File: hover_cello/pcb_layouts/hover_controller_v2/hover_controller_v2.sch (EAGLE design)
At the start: 32 parts, among them IC1 74LS279N, U1 L298

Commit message: placed all parts in .brd, started preliminary routing
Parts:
- added RN2: (no value), resistor-net:RN09
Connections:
- removed net N$10: CONTROL_IN.6, IC1C.R
- removed net N$11: CONTROL_IN.7, IC1D.S
- removed net N$12: CONTROL_IN.8, IC1D.R
- removed net N$5 (its old number): CONTROL_IN.1, IC1A.S1
- removed net N$6: CONTROL_IN.2, IC1A.R
- removed net N$7: CONTROL_IN.3, IC1B.S1
- removed net N$8: CONTROL_IN.4, IC1B.R
- removed net N$9: CONTROL_IN.5, IC1C.S
- new net R1: CONTROL_IN.2, IC1A.R, RN2.3
- new net R2: CONTROL_IN.4, IC1B.R, RN2.9
- new net R3: CONTROL_IN.6, IC1C.R, RN2.6
- new net R4: CONTROL_IN.8, IC1D.R, RN2.5
- new net S1: CONTROL_IN.1, IC1A.S1, RN2.2
- new net S2: CONTROL_IN.3, IC1B.S1, RN2.8
- new net S3: CONTROL_IN.5, IC1C.S, RN2.7
- new net S4: CONTROL_IN.7, IC1D.S, RN2.4
- net GND: now also VR1.1, VR2.1; no longer VR1.3, VR2.3
- net VCC: now also RN2.1, VR1.3, VR2.3; no longer VR1.1, VR2.1
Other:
- moved on the sheet: VR1, VR2
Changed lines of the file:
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@@
 <part name="C5" library="SparkFun-Capacitors" deviceset="CAP_POL" device="PTH2" value="220µf"/>
 <part name="GND15" library="SparkFun-Aesthetics" deviceset="GND" device=""/>
+<part name="RN2" library="resistor-net" library_urn="urn:adsk.eagle:library:343" deviceset="RN09" device=""/>
+<part name="SUPPLY9" library="SparkFun-Aesthetics" deviceset="VCC" device=""/>
 </parts>
 <sheets>
@@
 <instance part="U$1" gate="G$1" x="248.92" y="66.04" rot="R180"/>
 <instance part="POWER" gate="G$1" x="66.04" y="53.34"/>
-<instance part="VR1" gate="G$1" x="309.88" y="88.9" rot="R180"/>
-<instance part="VR2" gate="G$1" x="325.12" y="73.66" rot="R180"/>
+<instance part="VR1" gate="G$1" x="309.88" y="88.9" rot="MR0"/>
+<instance part="VR2" gate="G$1" x="325.12" y="73.66" rot="MR0"/>
 <instance part="SUPPLY3" gate="G$1" x="309.88" y="96.52"/>
 <instance part="SUPPLY4" gate="G$1" x="325.12" y="81.28"/>
@@
 <instance part="C5" gate="G$1" x="119.38" y="81.28" rot="R90"/>
 <instance part="GND15" gate="1" x="142.24" y="78.74"/>
+<instance part="RN2" gate="1" x="-33.02" y="124.46"/>
+<instance part="SUPPLY9" gate="G$1" x="-40.64" y="129.54"/>
 </instances>
 <busses>
@@
 </segment>
 </net>
-<net name="N$5" class="0">
+<net name="S1" class="0">
 <segment>
 <pinref part="CONTROL_IN" gate="1" pin="1"/>
@@
 <wire x1="22.86" y1="160.02" x2="53.34" y2="160.02" width="0.1524" layer="91"/>
 </segment>
-</net>
-<net name="N$6" class="0">
+<segment>
+<pinref part="RN2" gate="1" pin="2"/>
+<wire x1="-27.94" y1="124.46" x2="-27.94" y2="116.84" width="0.1524" layer="91"/>
+<label x="-27.94" y="116.84" size="1.778" layer="95" rot="R270" xref="yes"/>
+</segment>
+</net>
+<net name="R1" class="0">
 <segment>
 <pinref part="CONTROL_IN" gate="1" pin="2"/>
@@
 <wire x1="50.8" y1="152.4" x2="53.34" y2="152.4" width="0.1524" layer="91"/>
 </segment>
-</net>
-<net name="N$7" class="0">
+<segment>
+<pinref part="RN2" gate="1" pin="3"/>
+<wire x1="-22.86" y1="124.46" x2="-22.86" y2="114.3" width="0.1524" layer="91"/>
+<label x="-22.86" y="114.3" size="1.778" layer="95" rot="R270" xref="yes"/>
+</segment>
+</net>
+<net name="S2" class="0">
 <segment>
 <pinref part="CONTROL_IN" gate="1" pin="3"/>
@@
 <wire x1="48.26" y1="137.16" x2="53.34" y2="137.16" width="0.1524" layer="91"/>
 </segment>
-</net>
-<net name="N$8" class="0">
+<segment>
+<pinref part="RN2" gate="1" pin="8"/>
+<wire x1="2.54" y1="124.46" x2="2.54" y2="101.6" width="0.1524" layer="91"/>
+<label x="2.54" y="101.6" size="1.778" layer="95" rot="R270" xref="yes"/>
+</segment>
+</net>
+<net name="R2" class="0">
 <segment>
 <pinref part="CONTROL_IN" gate="1" pin="4"/>
@@
 <wire x1="45.72" y1="129.54" x2="53.34" y2="129.54" width="0.1524" layer="91"/>
 </segment>
-</net>
-<net name="N$9" class="0">
+<segment>
+<pinref part="RN2" gate="1" pin="9"/>
+<wire x1="7.62" y1="124.46" x2="7.62" y2="99.06" width="0.1524" layer="91"/>
+<label x="7.62" y="99.06" size="1.778" layer="95" rot="R270" xref="yes"/>
+</segment>
+</net>
+<net name="S3" class="0">
 <segment>
 <pinref part="CONTROL_IN" gate="1" pin="5"/>
@@
 <wire x1="43.18" y1="114.3" x2="53.34" y2="114.3" width="0.1524" layer="91"/>
 </segment>
-</net>
-<net name="N$10" class="0">
+<segment>
+<pinref part="RN2" gate="1" pin="7"/>
+<wire x1="-2.54" y1="124.46" x2="-2.54" y2="104.14" width="0.1524" layer="91"/>
+<label x="-2.54" y="104.14" size="1.778" layer="95" rot="R270" xref="yes"/>
+</segment>
+</net>
+<net name="R3" class="0">
 <segment>
 <pinref part="CONTROL_IN" gate="1" pin="6"/>
@@
 <wire x1="40.64" y1="106.68" x2="53.34" y2="106.68" width="0.1524" layer="91"/>
 </segment>
-</net>
-<net name="N$11" class="0">
+<segment>
+<pinref part="RN2" gate="1" pin="6"/>
+<wire x1="-7.62" y1="124.46" x2="-7.62" y2="106.68" width="0.1524" layer="91"/>
+<label x="-7.62" y="106.68" size="1.778" layer="95" rot="R270" xref="yes"/>
+</segment>
+</net>
+<net name="S4" class="0">
 <segment>
 <pinref part="CONTROL_IN" gate="1" pin="7"/>
@@
 <wire x1="38.1" y1="91.44" x2="53.34" y2="91.44" width="0.1524" layer="91"/>
 </segment>
-</net>
-<net name="N$12" class="0">
+<segment>
+<pinref part="RN2" gate="1" pin="4"/>
+<wire x1="-17.78" y1="124.46" x2="-17.78" y2="111.76" width="0.1524" layer="91"/>
+<label x="-17.78" y="111.76" size="1.778" layer="95" rot="R270" xref="yes"/>
+</segment>
+</net>
+<net name="R4" class="0">
 <segment>
 <pinref part="CONTROL_IN" gate="1" pin="8"/>
@@
 <pinref part="IC1" gate="D" pin="R"/>
 <wire x1="35.56" y1="83.82" x2="53.34" y2="83.82" width="0.1524" layer="91"/>
+</segment>
+<segment>
+<pinref part="RN2" gate="1" pin="5"/>
+<wire x1="-12.7" y1="124.46" x2="-12.7" y2="109.22" width="0.1524" layer="91"/>
+<label x="-12.7" y="109.22" size="1.778" layer="95" rot="R270" xref="yes"/>
 </segment>
 </net>
@@
 </segment>
 <segment>
-<pinref part="SUPPLY3" gate="G$1" pin="VCC"/>
-<pinref part="VR1" gate="G$1" pin="1"/>
-<wire x1="309.88" y1="96.52" x2="309.88" y2="93.98" width="0.1524" layer="91"/>
-</segment>
-<segment>
-<pinref part="SUPPLY4" gate="G$1" pin="VCC"/>
-<pinref part="VR2" gate="G$1" pin="1"/>
-<wire x1="325.12" y1="81.28" x2="325.12" y2="78.74" width="0.1524" layer="91"/>
-</segment>
-<segment>
 <pinref part="SUPPLY5" gate="G$1" pin="VCC"/>
 <wire x1="261.62" y1="106.68" x2="264.16" y2="106.68" width="0.1524" layer="91"/>
@@
 <pinref part="C2" gate="G$1" pin="+"/>
 <wire x1="2.54" y1="58.42" x2="2.54" y2="53.34" width="0.1524" layer="91"/>
+</segment>
+<segment>
+<pinref part="RN2" gate="1" pin="1"/>
+<pinref part="SUPPLY9" gate="G$1" pin="VCC"/>
+<wire x1="-38.1" y1="124.46" x2="-40.64" y2="124.46" width="0.1524" layer="91"/>
+<wire x1="-40.64" y1="124.46" x2="-40.64" y2="129.54" width="0.1524" layer="91"/>
+</segment>
+<segment>
+<pinref part="VR1" gate="G$1" pin="3"/>
+<pinref part="SUPPLY3" gate="G$1" pin="VCC"/>
+<wire x1="309.88" y1="93.98" x2="309.88" y2="96.52" width="0.1524" layer="91"/>
+</segment>
+<segment>
+<pinref part="VR2" gate="G$1" pin="3"/>
+<pinref part="SUPPLY4" gate="G$1" pin="VCC"/>
+<wire x1="325.12" y1="78.74" x2="325.12" y2="81.28" width="0.1524" layer="91"/>
 </segment>
 </net>
@@
 <wire x1="33.02" y1="30.48" x2="20.32" y2="30.48" width="0.1524" layer="91"/>
 <junction x="20.32" y="30.48"/>
-</segment>
-<segment>
-<pinref part="VR2" gate="G$1" pin="3"/>
-<pinref part="GND4" gate="1" pin="GND"/>
-<wire x1="325.12" y1="68.58" x2="325.12" y2="66.04" width="0.1524" layer="91"/>
-</segment>
-<segment>
-<pinref part="VR1" gate="G$1" pin="3"/>
-<pinref part="GND3" gate="1" pin="GND"/>
-<wire x1="309.88" y1="83.82" x2="309.88" y2="81.28" width="0.1524" layer="91"/>
 </segment>
 <segment>
@@
 <wire x1="124.46" y1="81.28" x2="142.24" y2="81.28" width="0.1524" layer="91"/>
 </segment>
+<segment>
+<pinref part="VR1" gate="G$1" pin="1"/>
+<pinref part="GND3" gate="1" pin="GND"/>
+<wire x1="309.88" y1="83.82" x2="309.88" y2="81.28" width="0.1524" layer="91"/>
+</segment>
+<segment>
+<pinref part="VR2" gate="G$1" pin="1"/>
+<pinref part="GND4" gate="1" pin="GND"/>
+<wire x1="325.12" y1="68.58" x2="325.12" y2="66.04" width="0.1524" layer="91"/>
+</segment>
 </net>
 <net name="CTRL_1" class="0">
@@
 <pinref part="VR1" gate="G$1" pin="2"/>
 <wire x1="269.24" y1="88.9" x2="304.8" y2="88.9" width="0.1524" layer="91"/>
-</segment>
-</net>
-<net name="N$19" class="0">
-<segment>
-<pinref part="VR2" gate="G$1" pin="2"/>
-<wire x1="320.04" y1="73.66" x2="264.16" y2="73.66" width="0.1524" layer="91"/>
-<pinref part="U$1" gate="G$1" pin="A2"/>
 </segment>
 </net>
@@
 </segment>
 </net>
+<net name="N$5" class="0">
+<segment>
+<pinref part="U$1" gate="G$1" pin="A2"/>
+<pinref part="VR2" gate="G$1" pin="2"/>
+<wire x1="264.16" y1="73.66" x2="320.04" y2="73.66" width="0.1524" layer="91"/>
+</segment>
+</net>

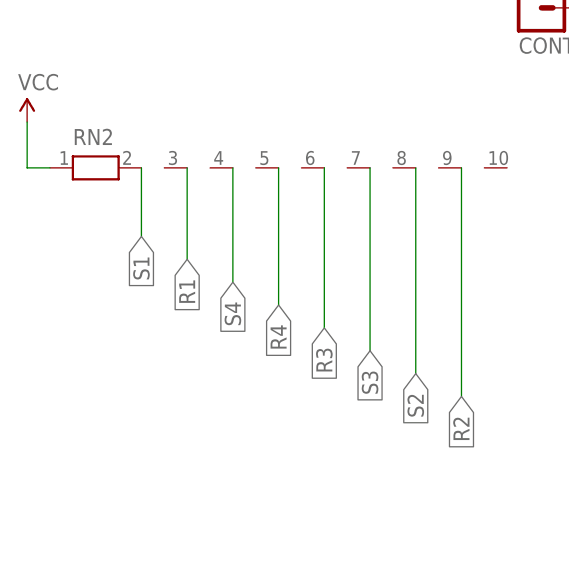
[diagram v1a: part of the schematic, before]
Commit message: wrote and tested V1.0 firmware for hover cello
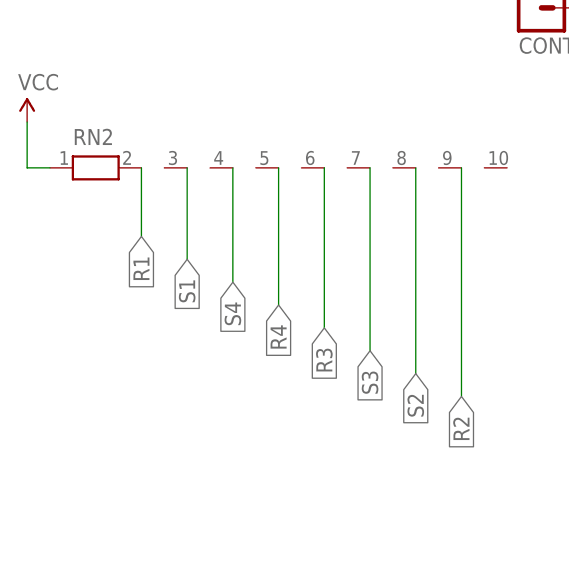
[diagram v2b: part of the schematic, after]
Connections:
- net R1: now also RN2.2; no longer RN2.3
- net S1: now also RN2.3; no longer RN2.2
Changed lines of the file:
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@@
 </segment>
 <segment>
-<pinref part="RN2" gate="1" pin="2"/>
-<wire x1="-27.94" y1="124.46" x2="-27.94" y2="116.84" width="0.1524" layer="91"/>
-<label x="-27.94" y="116.84" size="1.778" layer="95" rot="R270" xref="yes"/>
+<pinref part="RN2" gate="1" pin="3"/>
+<wire x1="-22.86" y1="124.46" x2="-22.86" y2="114.3" width="0.1524" layer="91"/>
+<label x="-22.86" y="114.3" size="1.778" layer="95" rot="R270" xref="yes"/>
 </segment>
 </net>
@@
 </segment>
 <segment>
-<pinref part="RN2" gate="1" pin="3"/>
-<wire x1="-22.86" y1="124.46" x2="-22.86" y2="114.3" width="0.1524" layer="91"/>
-<label x="-22.86" y="114.3" size="1.778" layer="95" rot="R270" xref="yes"/>
+<pinref part="RN2" gate="1" pin="2"/>
+<wire x1="-27.94" y1="124.46" x2="-27.94" y2="116.84" width="0.1524" layer="91"/>
+<label x="-27.94" y="116.84" size="1.778" layer="95" rot="R270" xref="yes"/>
 </segment>
 </net>
